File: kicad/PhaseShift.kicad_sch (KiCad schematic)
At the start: 0 parts

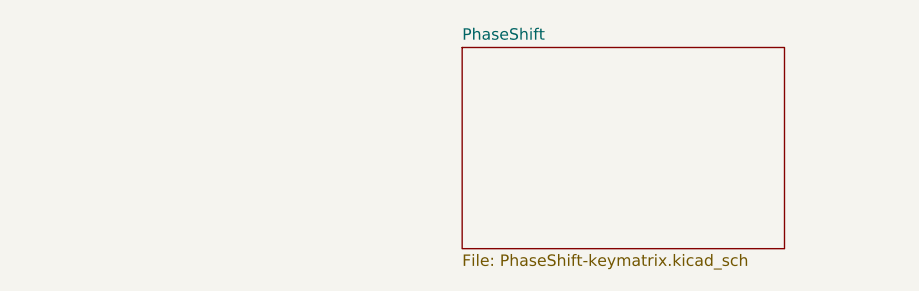
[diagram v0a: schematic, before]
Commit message: artwork for PhaseShift
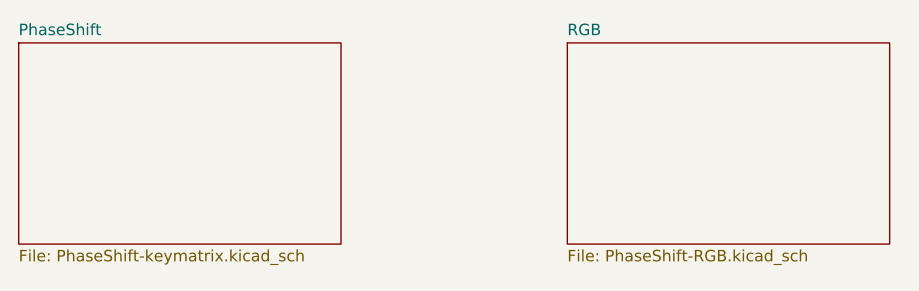
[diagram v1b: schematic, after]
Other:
- added sheet RGB (PhaseShift-RGB.kicad_sch)
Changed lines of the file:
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@@
 	(paper "A4")
 	(sheet
-		(at 76.2 165.862)
+		(at 87.884 165.354)
+		(size 35.814 22.352)
+		(exclude_from_sim no)
+		(in_bom yes)
+		(on_board yes)
+		(dnp no)
+		(fields_autoplaced yes)
+		(stroke
+			(width 0.1524)
+			(type solid)
+		)
+		(fill
+			(color 0 0 0 0.0000)
+		)
+		(property "Sheetname" "RGB"
+			(at 87.884 164.6424 0)
+			(effects
+				(font
+					(size 1.27 1.27)
+				)
+				(justify left bottom)
+			)
+		)
+		(property "Sheetfile" "PhaseShift-RGB.kicad_sch"
+			(at 87.884 188.2906 0)
+			(effects
+				(font
+					(size 1.27 1.27)
+				)
+				(justify left top)
+			)
+		)
+		(instances
+			(project "PhaseShift"
+				(path "/c7177d09-71a2-4de7-9a3e-bfc16a7f2797"
+					(page "2")
+				)
+			)
+		)
+	)
+	(sheet
+		(at 26.924 165.354)
 		(size 35.814 22.352)
 		(exclude_from_sim no)
@@
 		)
 		(property "Sheetname" "PhaseShift"
-			(at 76.2 165.1504 0)
+			(at 26.924 164.6424 0)
 			(effects
 				(font
@@
 		)
 		(property "Sheetfile" "PhaseShift-keymatrix.kicad_sch"
-			(at 76.2 188.7986 0)
+			(at 26.924 188.2906 0)
 			(effects
 				(font

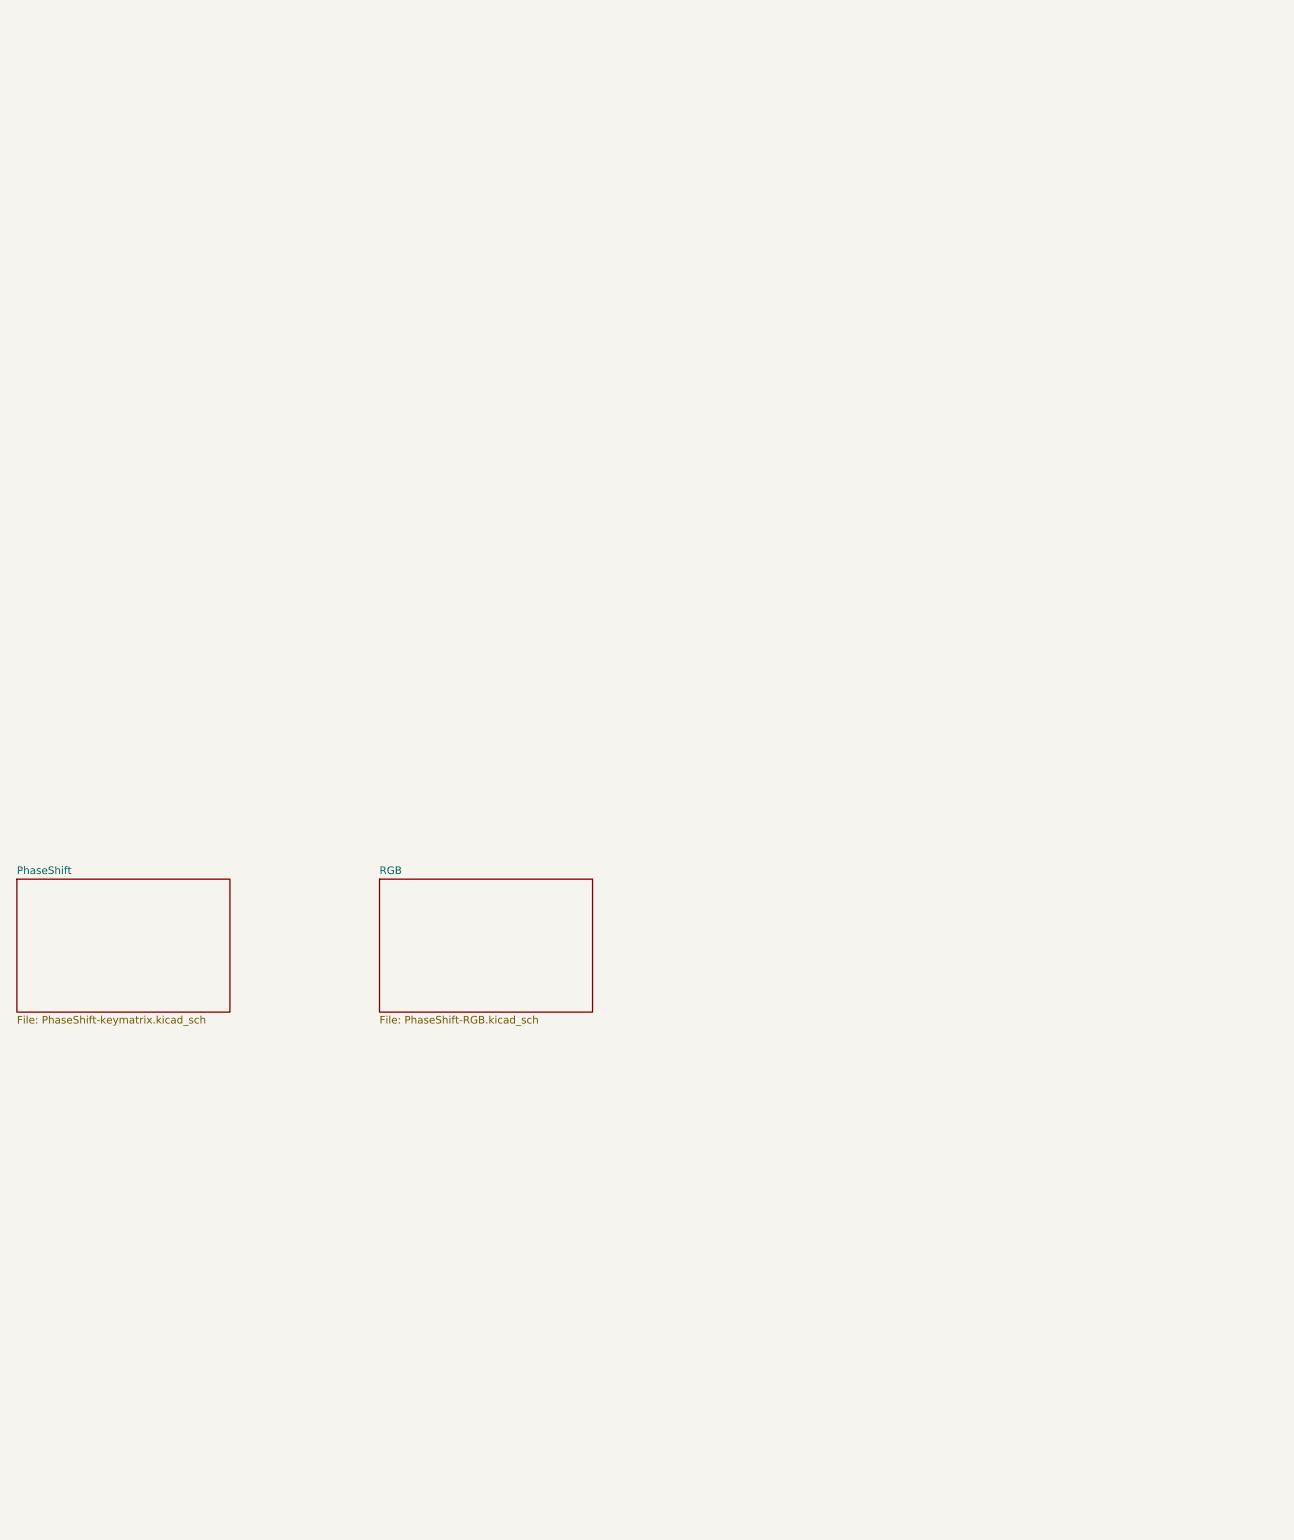
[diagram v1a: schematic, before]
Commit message: reorg schematic for PhaseShift
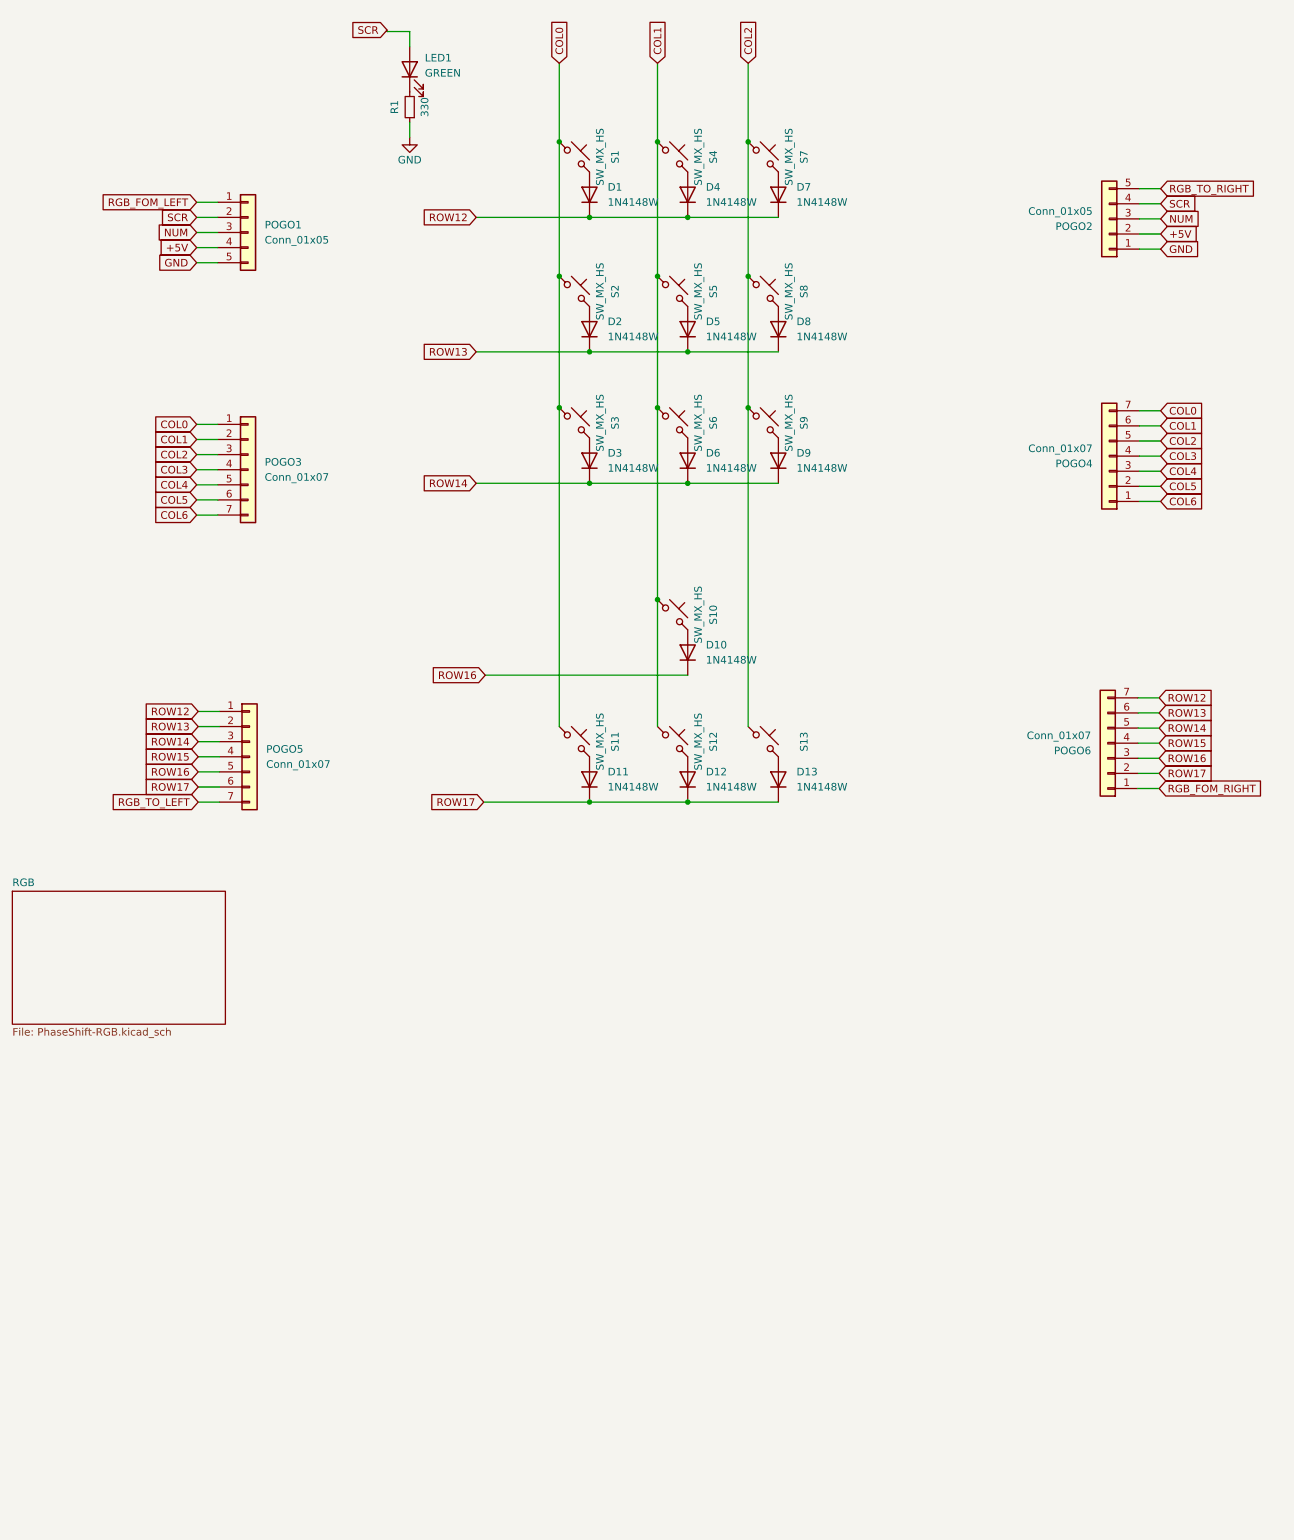
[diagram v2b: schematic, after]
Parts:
- added D1, D10, D11, D12, D13, D2, D3, D4, D5, D6, D7, D8, D9: 1N4148W, TB2086_SMD:D3_SMD, symbol Device:D
- added LED1: GREEN, LED_SMD:LED_0603_1608Metric_Pad1.05x0.95mm_HandSolder, symbol Device:LED
- added POGO1, POGO2: Conn_01x05, TB2086_MISC:Pogopin_1x05_P2.54mm_Curved, symbol Connector_Generic:Conn_01x05
- added POGO3, POGO4, POGO5, POGO6: Conn_01x07, TB2086_MISC:Pogopin_1x07_P2.54mm_Curved, symbol Connector_Generic:Conn_01x07
- added R1: 330, Resistor_SMD:R_0603_1608Metric, symbol Device:R_Small
- added S1, S10, S11, S12, S2, S3, S4, S5, S6, S7, S8, S9: SW_MX_HS, TB2086_KEYSWITCH:SW_MX_HS_1u, symbol TB2086_KEYSWITCH:SW_MX_HS
- added S13: SW_MX_HS_1u, TB2086_KEYSWITCH:SW_MX_HS_1u, symbol TB2086_KEYSWITCH:SW_MX_HS
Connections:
- new net: D7.2 (A), S7.1
- new net: D9.2 (A), S9.1
- new net: D1.2 (A), S1.1
- new net: D12.2 (A), S12.1
- new net: D10.2 (A), S10.1
- new net: D3.2 (A), S3.1
- new net: D13.2 (A), S13.1
- new net: D6.2 (A), S6.1
- new net: LED1.1 (K), R1.2
- new net: D2.2 (A), S2.1
- new net: D11.2 (A), S11.1
- new net: D4.2 (A), S4.1
- new net: D8.2 (A), S8.1
- new net: D5.2 (A), S5.1
- new net +5V: POGO1.4 (Pin_4), POGO2.2 (Pin_2)
- new net COL0: POGO3.1 (Pin_1), POGO4.7 (Pin_7), S1.2, S11.2, S2.2, S3.2
- new net COL1: POGO3.2 (Pin_2), POGO4.6 (Pin_6), S10.2, S12.2, S4.2, S5.2, S6.2
- new net COL2: POGO3.3 (Pin_3), POGO4.5 (Pin_5), S13.2, S7.2, S8.2, S9.2
- new net COL3: POGO3.4 (Pin_4), POGO4.4 (Pin_4)
- new net COL4: POGO3.5 (Pin_5), POGO4.3 (Pin_3)
- new net COL5: POGO3.6 (Pin_6), POGO4.2 (Pin_2)
- new net COL6: POGO3.7 (Pin_7), POGO4.1 (Pin_1)
- new net GND: POGO1.5 (Pin_5), POGO2.1 (Pin_1), R1.1
- new net NUM: POGO1.3 (Pin_3), POGO2.3 (Pin_3)
- new net RGB_FOM_LEFT: POGO1.1 (Pin_1)
- new net RGB_FOM_RIGHT: POGO6.1 (Pin_1)
- new net RGB_TO_LEFT: POGO5.7 (Pin_7)
- new net RGB_TO_RIGHT: POGO2.5 (Pin_5)
- new net ROW12: D1.1 (K), D4.1 (K), D7.1 (K), POGO5.1 (Pin_1), POGO6.7 (Pin_7)
- new net ROW13: D2.1 (K), D5.1 (K), D8.1 (K), POGO5.2 (Pin_2), POGO6.6 (Pin_6)
- new net ROW14: D3.1 (K), D6.1 (K), D9.1 (K), POGO5.3 (Pin_3), POGO6.5 (Pin_5)
- new net ROW15: POGO5.4 (Pin_4), POGO6.4 (Pin_4)
- new net ROW16: D10.1 (K), POGO5.5 (Pin_5), POGO6.3 (Pin_3)
- new net ROW17: D11.1 (K), D12.1 (K), D13.1 (K), POGO5.6 (Pin_6), POGO6.2 (Pin_2)
- new net SCR: LED1.2 (A), POGO1.2 (Pin_2), POGO2.4 (Pin_4)
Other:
- removed sheet PhaseShift

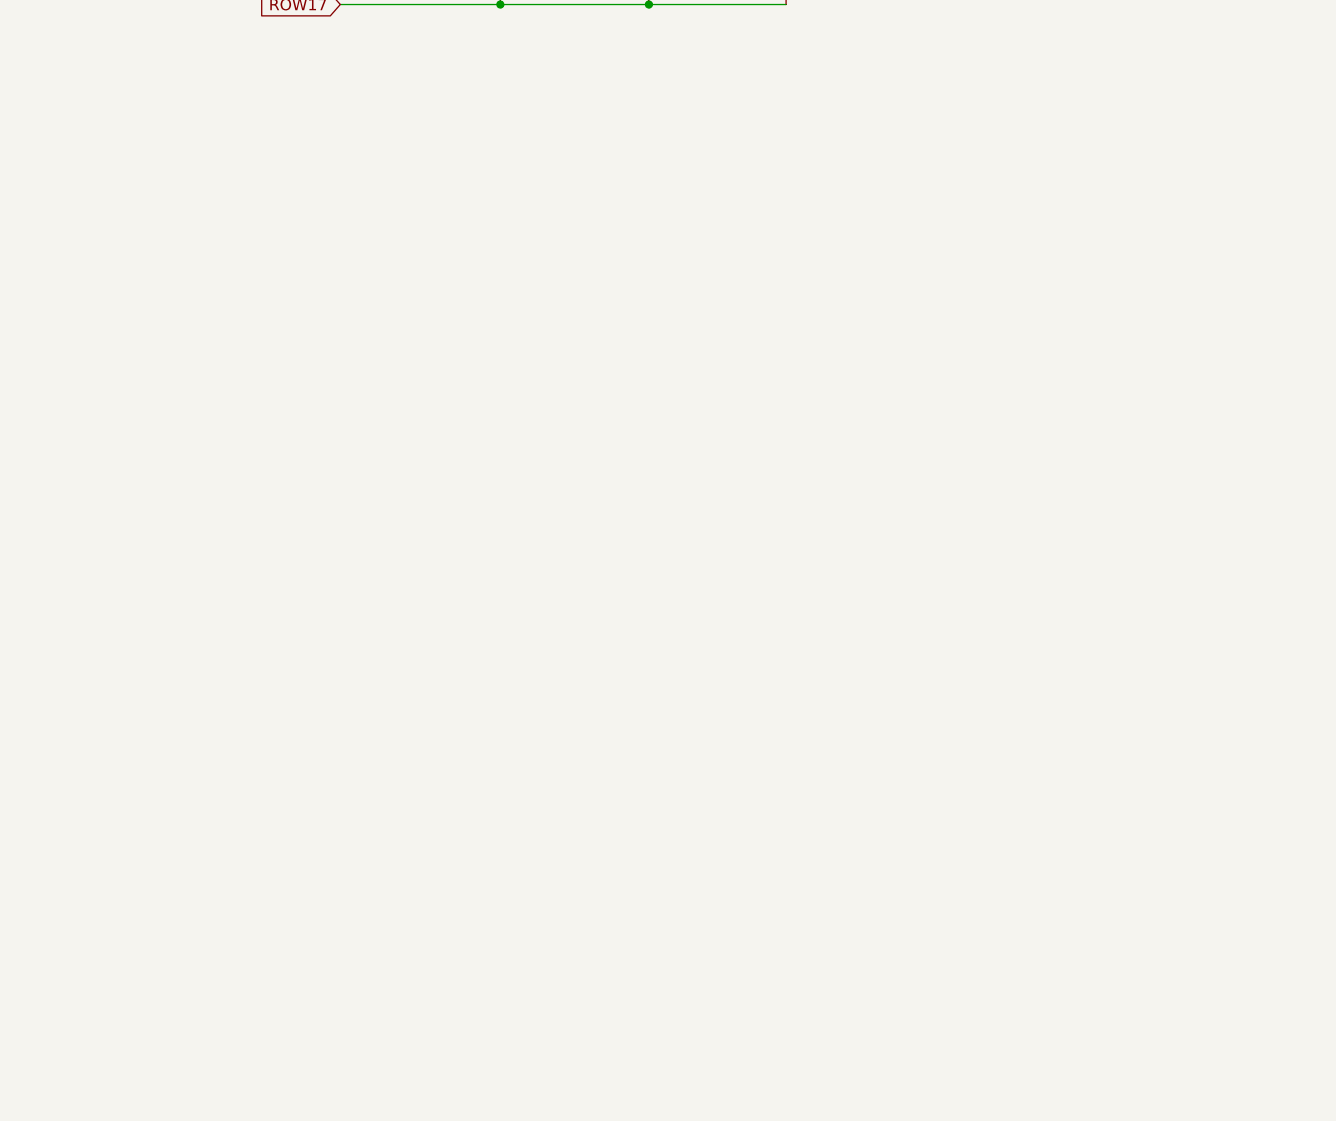
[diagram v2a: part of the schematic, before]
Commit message: side bars
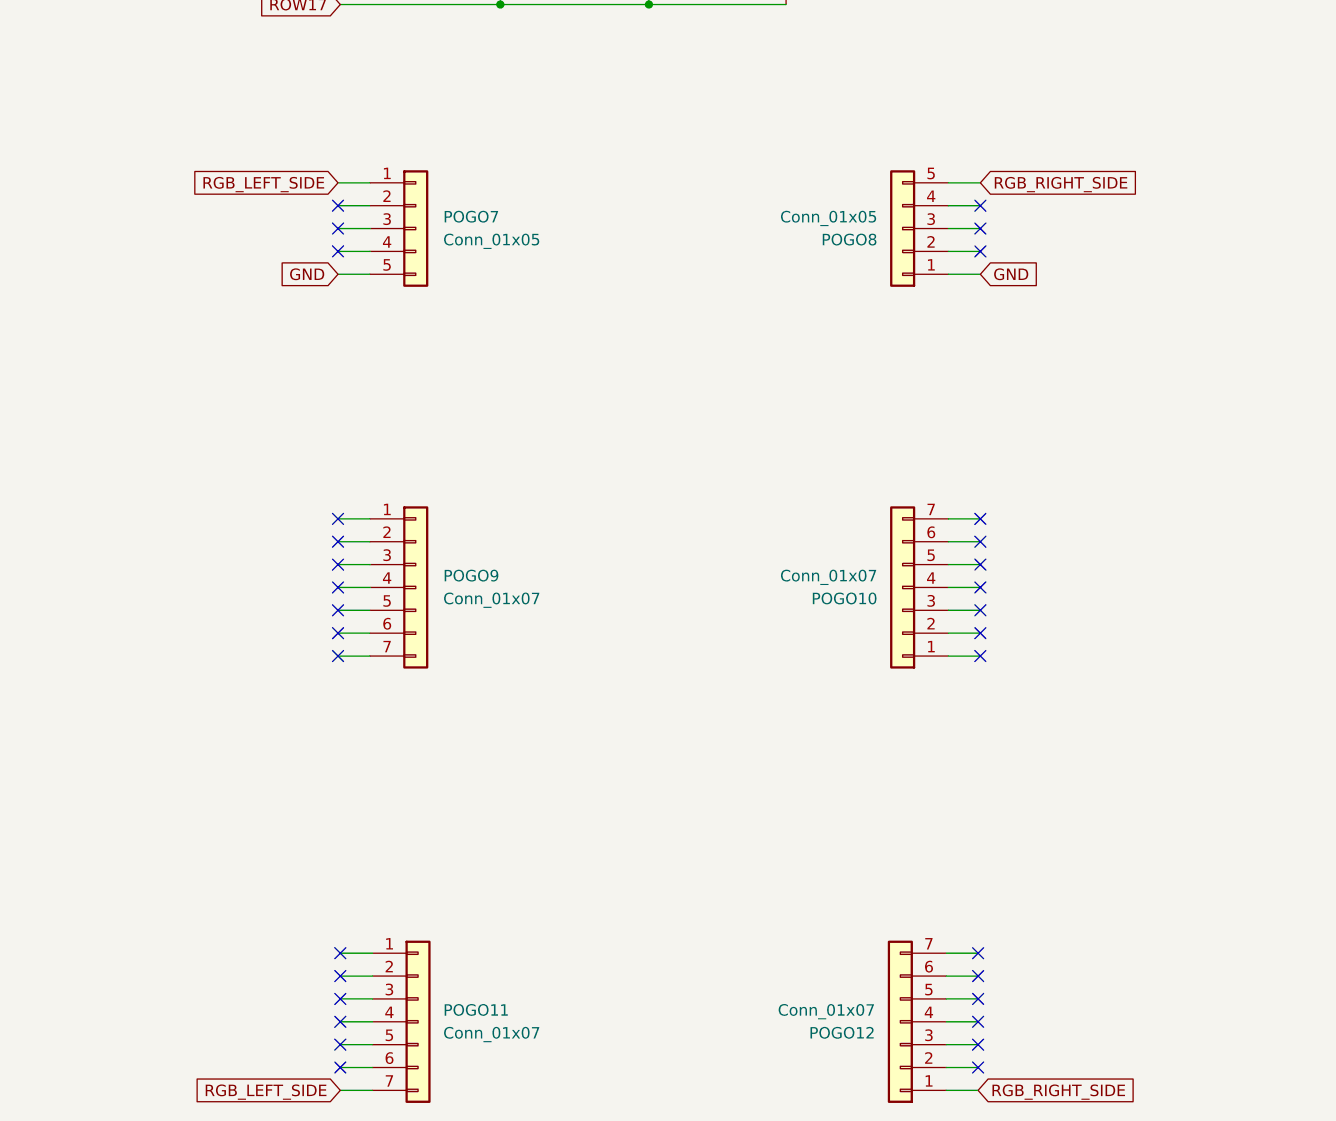
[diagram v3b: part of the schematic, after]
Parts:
- added POGO10, POGO11, POGO12, POGO9: Conn_01x07, TB2086_MISC:Pogopin_1x07_P2.54mm, symbol Connector_Generic:Conn_01x07
- added POGO7, POGO8: Conn_01x05, TB2086_MISC:Pogopin_1x05_P2.54mm, symbol Connector_Generic:Conn_01x05
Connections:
- net GND: now also POGO7.5 (Pin_5), POGO8.1 (Pin_1)
- new net RGB_LEFT_SIDE: POGO11.7 (Pin_7), POGO7.1 (Pin_1)
- new net RGB_RIGHT_SIDE: POGO12.1 (Pin_1), POGO8.5 (Pin_5)
- no-connect marks 0 -> 32
